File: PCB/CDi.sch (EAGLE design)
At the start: 9 parts, among them U1 SN74AHCT125N, U2 SN74AHCT125N

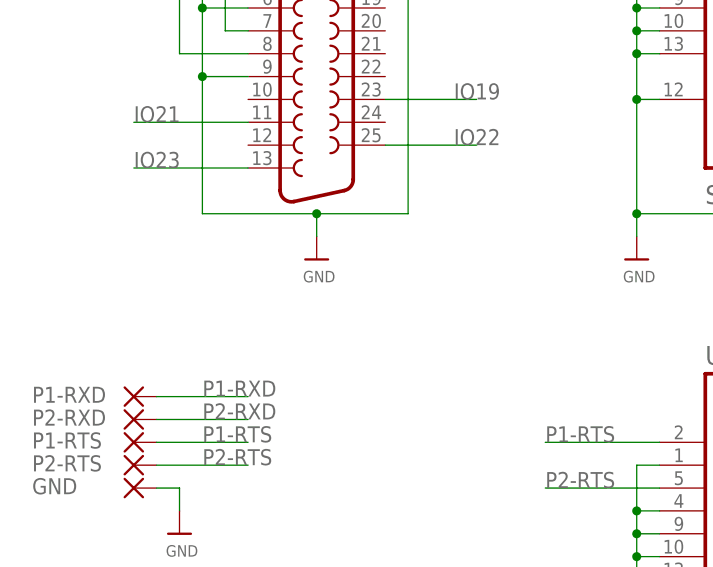
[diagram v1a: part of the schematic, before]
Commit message: Added exposed GND plane at DB25 anchors
All PCBs have been update to have exposed GND plane pads for the DB25 anchor points.

This resolves Issue 54
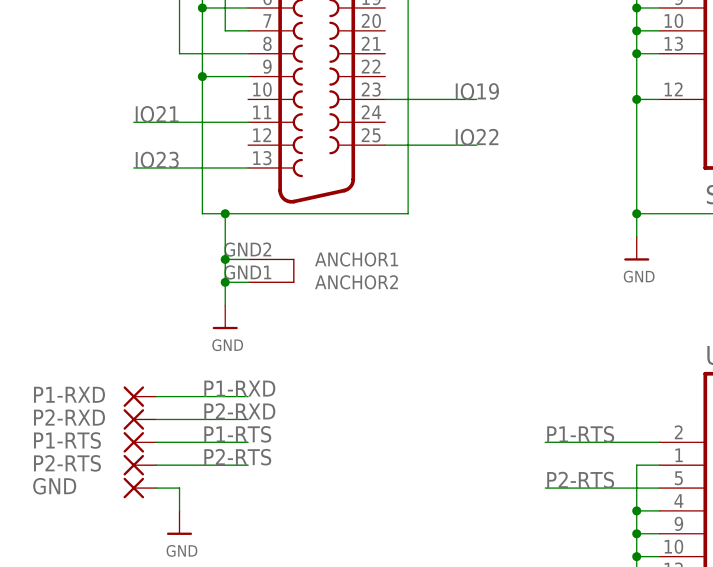
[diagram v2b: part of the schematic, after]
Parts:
- X1: device SparkFun-Retired:DB25_FEMALEH -> SparkFun-Retired:DB25_FEMALEHP
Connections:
- net GND: now also X1.ANCHOR1, X1.ANCHOR2
